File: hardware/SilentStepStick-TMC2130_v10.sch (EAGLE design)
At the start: 26 parts, among them IC1 TMC2100-LA, X1 PASSER-07, X2 PASSER-07

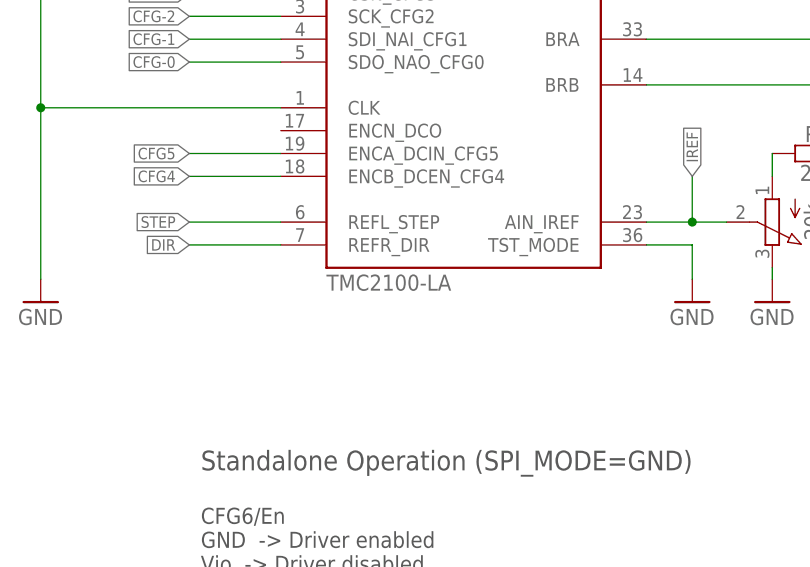
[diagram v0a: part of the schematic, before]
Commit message: updated schematics
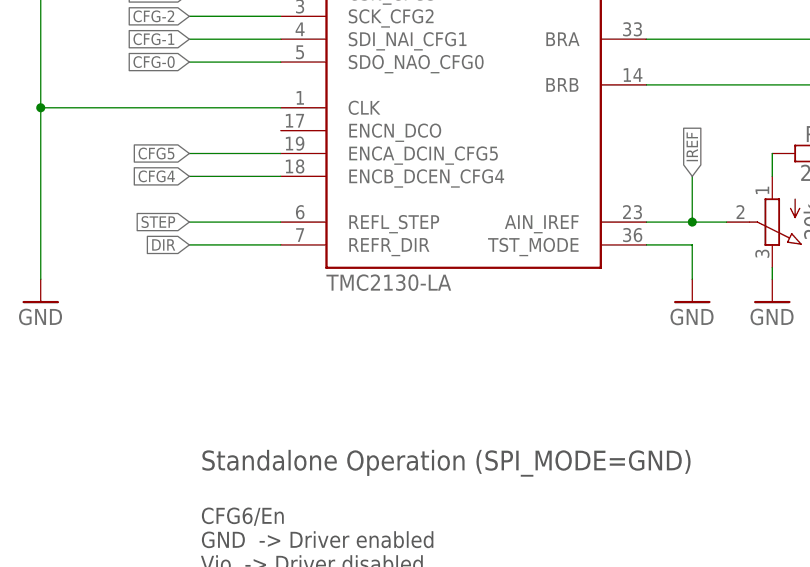
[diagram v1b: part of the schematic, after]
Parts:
- IC1: value TMC2100-LA -> TMC2130-LA; device we-chip:TMC2100-LA -> we-chip:TMC21X0-LA
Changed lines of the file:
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@@
 <?xml version="1.0" encoding="utf-8"?>
 <!DOCTYPE eagle SYSTEM "eagle.dtd">
-<eagle version="7.5.0">
+<eagle version="7.6.0">
 <drawing>
 <settings>
@@
 <setting verticaltext="up"/>
 </settings>
-<grid distance="0.05" unitdist="inch" unit="inch" style="lines" multiple="1" display="yes" altdistance="0.025" altunitdist="inch" altunit="inch"/>
+<grid distance="0.1" unitdist="inch" unit="inch" style="lines" multiple="1" display="no" altdistance="0.01" altunitdist="inch" altunit="inch"/>
 <layers>
 <layer number="1" name="Top" color="4" fill="1" visible="no" active="no"/>
@@
 <part name="R5" library="we-rcl" deviceset="RESISTOR" device="-0402" value="20k"/>
 <part name="R1" library="we-rcl" deviceset="RESISTOR" device="-0402" value="2R2"/>
-<part name="IC1" library="we-chip" deviceset="TMC2100" device="-LA"/>
+<part name="IC1" library="we-chip" deviceset="TMC21X0" device="-LA" value="TMC2130-LA"/>
 <part name="GND17" library="supply1" deviceset="GND" device=""/>
 <part name="SPI" library="we-rcl" deviceset="JUMPER2" device="-0402-NC"/>
